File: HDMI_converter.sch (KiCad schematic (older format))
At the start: 106 parts, among them J2 46756-1001, Q1 BSS138APW, Q2 BSS138APW, Q3 BSS138APW, Q4 BSS138APW, U2 LT9611, U3 TXB0104RUT, U4 NTS0102GT, Y2 ABM8G-24.000MHZ-18-D2Y-T

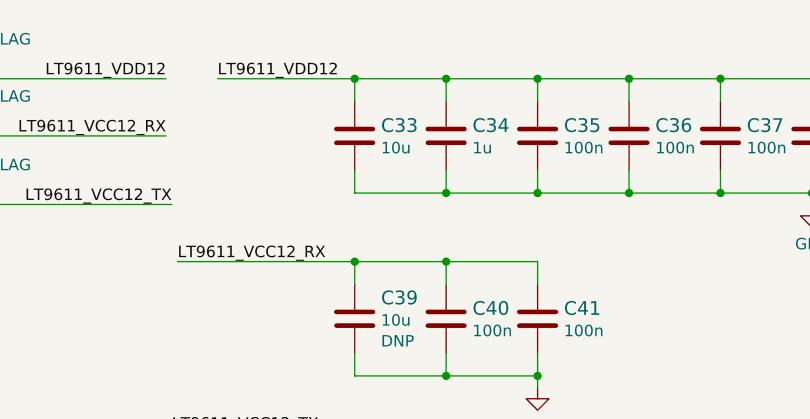
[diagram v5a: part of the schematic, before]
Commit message: Restore pcb with grouped parts. Change C33 to DNP
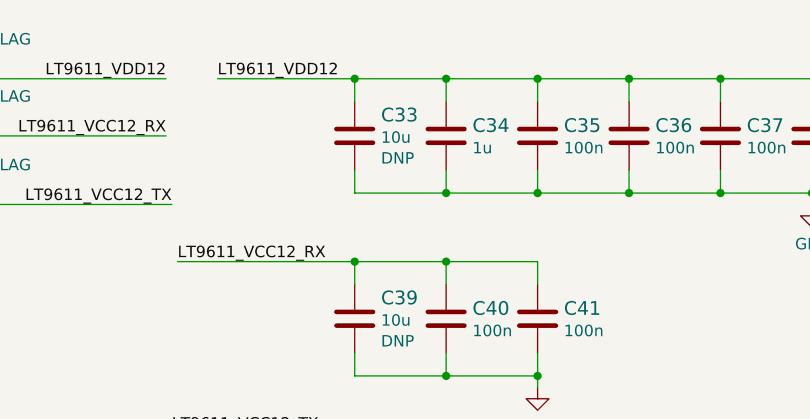
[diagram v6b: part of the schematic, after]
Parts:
- C33: DNP (none) -> DNP
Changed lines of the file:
@@
 U 1 1 627857E5
 P 8450 1150
-F 0 "C33" H 8565 1195 60  0000 L CNN
+F 0 "C33" H 8565 1241 60  0000 L CNN
 F 1 "C_10u_0402" H 8450 1000 60  0001 C CNN
 F 2 "sa800u-baseboard-hw-footprints:0402-cap" H 8650 1350 60  0001 L CNN
@@
 F 4 "MURATA" H 8650 1550 60  0001 L CNN "Manufacturer"
 F 5 "GRM155R60J106ME44D" H 8650 1450 60  0001 L CNN "MPN"
-F 6 "10u" H 8565 1097 50  0000 L CNN "Val"
+F 6 "10u" H 8565 1143 50  0000 L CNN "Val"
+F 7 "DNP" H 8565 1052 50  0000 L CNN "DNP"
 	1    8450 1150
 	1    0    0    -1

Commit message: Update 510R resistors
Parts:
- removed R134, R54, R56, R57, R58, R60, R61, R62: R_510R_0402, sa800u-baseboard-hw-footprints:0402-res, symbol sa800u-baseboard-hw:R_510R_0402
- added C151: C_100n_0402, sa800u-baseboard-hw-footprints:0402-cap, symbol sa800u-baseboard-hw:C_100n_0402
- added R134, R137, R57, R58, R60, R61, R62, R87: R_510R_0402, antmicro-footprints:0402-res, symbol antmicroResistors0402:R_510R_0402
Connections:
- wire segments 479 -> 483
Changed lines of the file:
@@
 Wire Wire Line
 	8850 1400 8450 1400
-Wire Wire Line
-	10450 1400 10450 1450
 $Comp
 L sa800u-baseboard-hw:GND #PWR019
 U 1 1 6271E8F1
-P 10450 1450
-F 0 "#PWR019" H 10450 1200 50  0001 C CNN
-F 1 "GND" H 10455 1277 50  0000 C CNN
-F 2 "" H 10450 1450 50  0001 C CNN
-F 3 "" H 10450 1450 50  0001 C CNN
-	1    10450 1450
+P 10850 1425
+F 0 "#PWR019" H 10850 1175 50  0001 C CNN
+F 1 "GND" H 10855 1252 50  0000 C CNN
+F 2 "" H 10850 1425 50  0001 C CNN
+F 3 "" H 10850 1425 50  0001 C CNN
+	1    10850 1425
 	1    0    0    -1
 $EndComp
@@
 	9325 6100 11600 6100
 Wire Wire Line
-	12475 6650 12475 6550
-Wire Wire Line
 	14575 6650 14575 6550
 Connection ~ 13525 6650
@@
 Wire Wire Line
 	3450 4125 3450 4025
-Connection ~ 10450 1400
 Connection ~ 8450 1700
 Connection ~ 8450 900
@@
 Wire Wire Line
 	2950 2475 3700 2475
-Text Label 2600 4025 0    50   ~ 0
+Text Label 2550 4425 0    50   ~ 0
 LT9611_VCC33_IO
-Text Label 2550 4425 0    50   ~ 0
+Text Label 2550 4025 0    50   ~ 0
 LT9611_VCC33_RX
 Text Label 2575 4725 0    50   ~ 0
@@
 	2550 4425 3450 4425
 Wire Wire Line
-	2600 4025 3450 4025
+	2550 4025 3450 4025
 Text Label 8600 4600 0    50   ~ 0
 LT9611_VCC33_TX
@@
 Wire Wire Line
 	4800 4925 5625 4925
-$Comp
-L sa800u-baseboard-hw:R_510R_0402 R54
-U 1 1 62E016CC
+Text GLabel 1375 6325 0    50   Input ~ 0
+DSI1_LN0_P
+$Comp
+L sa800u-baseboard-hw:C_100n_0402 C151
+U 1 1 620737ED
+P 10850 1150
+F 0 "C151" H 10965 1195 60  0000 L CNN
+F 1 "C_100n_0402" H 10850 1000 60  0001 C CNN
+F 2 "sa800u-baseboard-hw-footprints:0402-cap" H 11050 1350 60  0001 L CNN
+F 3 "" H 10850 1150 50  0001 C CNN
+F 4 "Walsin" H 11050 1550 60  0001 L CNN "Manufacturer"
+F 5 "0402X104K6R3CT" H 11050 1450 60  0001 L CNN "MPN"
+F 6 "100n" H 10965 1097 50  0000 L CNN "Val"
+	1    10850 1150
+	1    0    0    -1
+$EndComp
+Wire Wire Line
+	10850 900  10850 1000
+Wire Wire Line
+	10450 900  10850 900
+Wire Wire Line
+	10450 1400 10850 1400
+Connection ~ 10850 1400
+Wire Wire Line
+	10850 1400 10850 1425
+Wire Wire Line
+	10850 1300 10850 1400
+Connection ~ 10450 1400
+Connection ~ 10450 900
+$Comp
+L antmicroResistors0402:R_510R_0402 R57
+U 1 1 622FF01E
 P 12475 6400
-F 0 "R54" V 12430 6470 60  0000 L CNN
+F 0 "R57" V 12430 6470 60  0000 L CNN
 F 1 "R_510R_0402" H 12475 6250 60  0001 C CNN
-F 2 "sa800u-baseboard-hw-footprints:0402-res" H 12675 6600 60  0001 L CNN
+F 2 "antmicro-footprints:0402-res" H 12675 6600 60  0001 L CNN
 F 3 "" H 12475 6400 50  0001 C CNN
 F 4 "Yageo" H 12675 6800 60  0001 L CNN "Manufacturer"
@@
 	0    1    1    0
 $EndComp
-$Comp
-L sa800u-baseboard-hw:R_510R_0402 R56
-U 1 1 62E4D5ED
+Wire Wire Line
+	12475 6550 12475 6650
+$Comp
+L antmicroResistors0402:R_510R_0402 R58
+U 1 1 62395D6F
 P 12825 6400
-F 0 "R56" V 12780 6470 60  0000 L CNN
+F 0 "R58" V 12780 6470 60  0000 L CNN
 F 1 "R_510R_0402" H 12825 6250 60  0001 C CNN
-F 2 "sa800u-baseboard-hw-footprints:0402-res" H 13025 6600 60  0001 L CNN
+F 2 "antmicro-footprints:0402-res" H 13025 6600 60  0001 L CNN
 F 3 "" H 12825 6400 50  0001 C CNN
 F 4 "Yageo" H 13025 6800 60  0001 L CNN "Manufacturer"
@@
 $EndComp
 $Comp
-L sa800u-baseboard-hw:R_510R_0402 R57
-U 1 1 62E92C49
+L antmicroResistors0402:R_510R_0402 R60
+U 1 1 623DE328
 P 13175 6400
-F 0 "R57" V 13130 6470 60  0000 L CNN
+F 0 "R60" V 13130 6470 60  0000 L CNN
 F 1 "R_510R_0402" H 13175 6250 60  0001 C CNN
-F 2 "sa800u-baseboard-hw-footprints:0402-res" H 13375 6600 60  0001 L CNN
+F 2 "antmicro-footprints:0402-res" H 13375 6600 60  0001 L CNN
 F 3 "" H 13175 6400 50  0001 C CNN
 F 4 "Yageo" H 13375 6800 60  0001 L CNN "Manufacturer"
@@
 $EndComp
 $Comp
-L sa800u-baseboard-hw:R_510R_0402 R58
-U 1 1 62E92C52
+L antmicroResistors0402:R_510R_0402 R61
+U 1 1 623DE331
 P 13525 6400
-F 0 "R58" V 13480 6470 60  0000 L CNN
+F 0 "R61" V 13480 6470 60  0000 L CNN
 F 1 "R_510R_0402" H 13525 6250 60  0001 C CNN
-F 2 "sa800u-baseboard-hw-footprints:0402-res" H 13725 6600 60  0001 L CNN
+F 2 "antmicro-footprints:0402-res" H 13725 6600 60  0001 L CNN
 F 3 "" H 13525 6400 50  0001 C CNN
 F 4 "Yageo" H 13725 6800 60  0001 L CNN "Manufacturer"
@@
 $EndComp
 $Comp
-L sa800u-baseboard-hw:R_510R_0402 R60
-U 1 1 62ED7826
+L antmicroResistors0402:R_510R_0402 R62
+U 1 1 62423F3E
 P 13875 6400
-F 0 "R60" V 13830 6470 60  0000 L CNN
+F 0 "R62" V 13830 6470 60  0000 L CNN
 F 1 "R_510R_0402" H 13875 6250 60  0001 C CNN
-F 2 "sa800u-baseboard-hw-footprints:0402-res" H 14075 6600 60  0001 L CNN
+F 2 "antmicro-footprints:0402-res" H 14075 6600 60  0001 L CNN
 F 3 "" H 13875 6400 50  0001 C CNN
 F 4 "Yageo" H 14075 6800 60  0001 L CNN "Manufacturer"
@@
 $EndComp
 $Comp
-L sa800u-baseboard-hw:R_510R_0402 R61
-U 1 1 62ED782F
+L antmicroResistors0402:R_510R_0402 R87
+U 1 1 62423F47
 P 14225 6400
-F 0 "R61" V 14180 6470 60  0000 L CNN
+F 0 "R87" V 14180 6470 60  0000 L CNN
 F 1 "R_510R_0402" H 14225 6250 60  0001 C CNN
-F 2 "sa800u-baseboard-hw-footprints:0402-res" H 14425 6600 60  0001 L CNN
+F 2 "antmicro-footprints:0402-res" H 14425 6600 60  0001 L CNN
 F 3 "" H 14225 6400 50  0001 C CNN
 F 4 "Yageo" H 14425 6800 60  0001 L CNN "Manufacturer"
@@
 $EndComp
 $Comp
-L sa800u-baseboard-hw:R_510R_0402 R62
-U 1 1 62F1C359
+L antmicroResistors0402:R_510R_0402 R134
+U 1 1 624698FA
 P 14575 6400
-F 0 "R62" V 14530 6470 60  0000 L CNN
+F 0 "R134" V 14530 6470 60  0000 L CNN
 F 1 "R_510R_0402" H 14575 6250 60  0001 C CNN
-F 2 "sa800u-baseboard-hw-footprints:0402-res" H 14775 6600 60  0001 L CNN
+F 2 "antmicro-footprints:0402-res" H 14775 6600 60  0001 L CNN
 F 3 "" H 14575 6400 50  0001 C CNN
 F 4 "Yageo" H 14775 6800 60  0001 L CNN "Manufacturer"
@@
 $EndComp
 $Comp
-L sa800u-baseboard-hw:R_510R_0402 R134
-U 1 1 62F1C362
+L antmicroResistors0402:R_510R_0402 R137
+U 1 1 62469903
 P 14925 6400
-F 0 "R134" V 14880 6470 60  0000 L CNN
+F 0 "R137" V 14880 6470 60  0000 L CNN
 F 1 "R_510R_0402" H 14925 6250 60  0001 C CNN
-F 2 "sa800u-baseboard-hw-footprints:0402-res" H 15125 6600 60  0001 L CNN
+F 2 "antmicro-footprints:0402-res" H 15125 6600 60  0001 L CNN
 F 3 "" H 14925 6400 50  0001 C CNN
 F 4 "Yageo" H 15125 6800 60  0001 L CNN "Manufacturer"
@@
 	0    1    1    0
 $EndComp
-Text GLabel 1375 6325 0    50   Input ~ 0
-DSI1_LN0_P
 $EndSCHEMATC

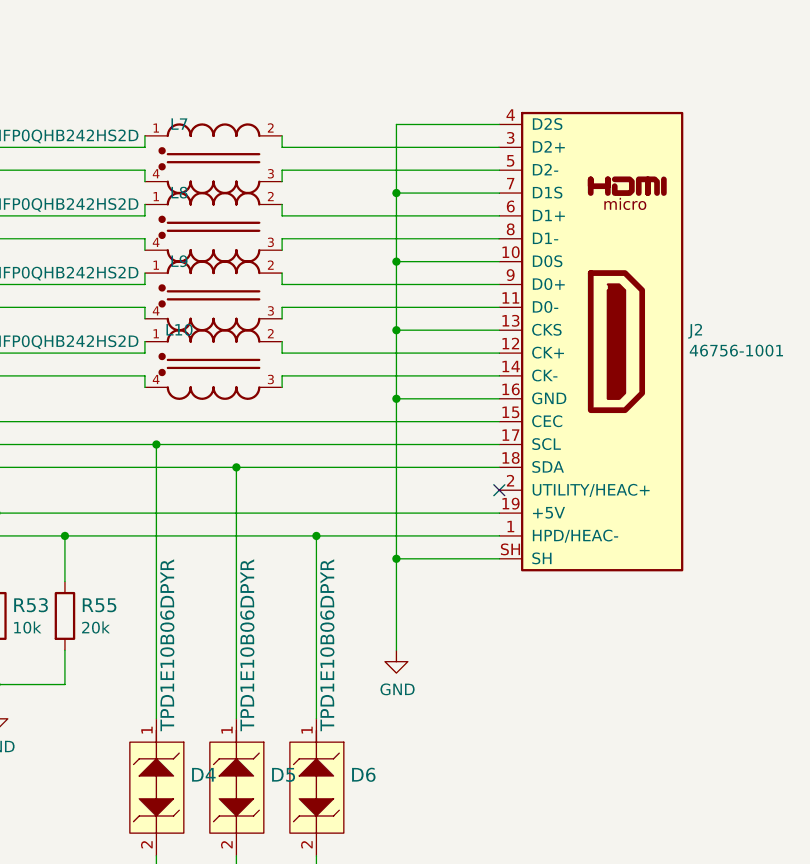
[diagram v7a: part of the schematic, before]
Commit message: Add names to nets connected to HDMI connector
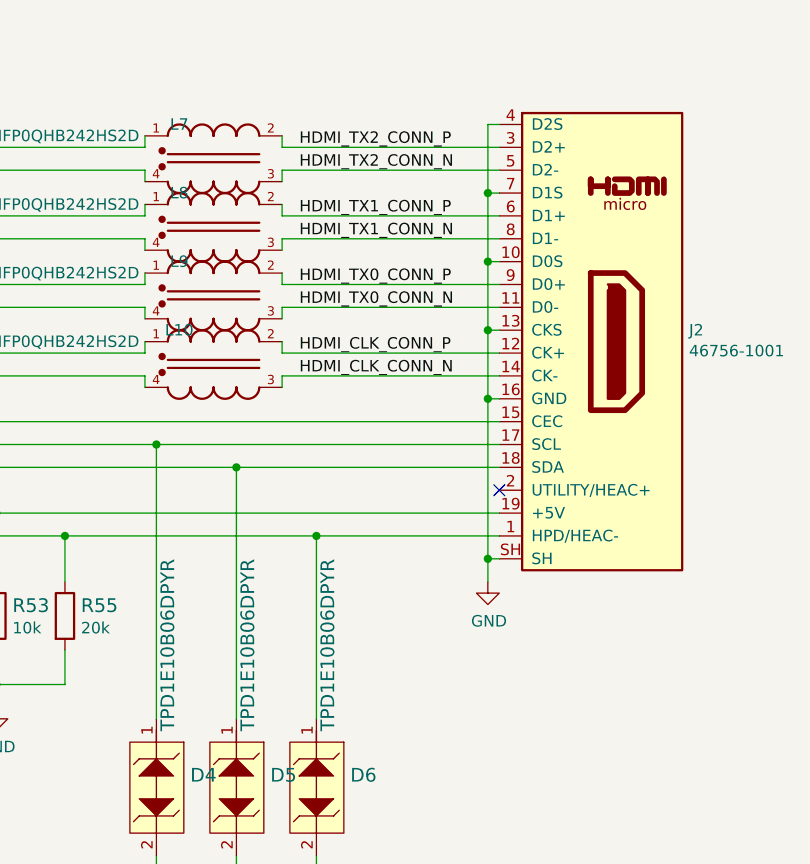
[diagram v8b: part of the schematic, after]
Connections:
- net HDMI_TX0_CONN_N: now reaches J2.11 (D0-), L9.3
- net HDMI_CLK_CONN_P: now reaches J2.12 (CK+), L10.2
- net HDMI_CLK_CONN_N: now reaches J2.14 (CK-), L10.3
- net HDMI_TX2_CONN_P: now reaches J2.3 (D2+), L7.2
- net HDMI_TX2_CONN_N: now reaches J2.5 (D2-), L7.3
- net HDMI_TX1_CONN_P: now reaches J2.6 (D1+), L8.2
- net HDMI_TX1_CONN_N: now reaches J2.8 (D1-), L8.3
- net HDMI_TX0_CONN_P: now reaches J2.9 (D0+), L9.2
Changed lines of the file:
@@
 HDMI_CLK_N
 Wire Wire Line
-	14750 1100 14300 1100
-Wire Wire Line
-	14300 1100 14300 1400
-Wire Wire Line
-	14750 3000 14300 3000
+	14750 3000 14700 3000
 Wire Wire Line
 	14750 1200 13800 1200
@@
 $EndComp
 Wire Wire Line
-	14750 1400 14300 1400
-Connection ~ 14300 1400
-Wire Wire Line
-	14300 1400 14300 1700
+	14750 1400 14700 1400
 Wire Wire Line
 	14750 1500 13800 1500
@@
 $EndComp
 Wire Wire Line
-	14750 1700 14300 1700
-Connection ~ 14300 1700
-Wire Wire Line
-	14300 1700 14300 2000
-Wire Wire Line
 	14750 1800 13800 1800
 Wire Wire Line
@@
 	1    0    0    -1
 $EndComp
-Wire Wire Line
-	14750 2000 14300 2000
 Wire Wire Line
 	14750 2100 13800 2100
@@
 	1    0    0    -1
 $EndComp
-Wire Wire Line
-	14300 2000 14300 2300
-Connection ~ 14300 2000
-Connection ~ 14300 3000
 Text Label 11850 2800 0    50   ~ 0
 5V_HDMI
@@
 Wire Wire Line
 	11850 2800 12550 2800
-Wire Wire Line
-	14300 3000 14300 3400
 $Comp
 L sa800u-baseboard-hw:GND #PWR035
 U 1 1 62C195C0
-P 14300 3400
-F 0 "#PWR035" H 14300 3150 50  0001 C CNN
-F 1 "GND" H 14305 3227 50  0000 C CNN
-F 2 "" H 14300 3400 50  0001 C CNN
-F 3 "" H 14300 3400 50  0001 C CNN
-	1    14300 3400
-	1    0    0    -1
-$EndComp
-Wire Wire Line
-	14750 2300 14300 2300
-Connection ~ 14300 2300
-Wire Wire Line
-	14300 2300 14300 3000
+P 14700 3100
+F 0 "#PWR035" H 14700 2850 50  0001 C CNN
+F 1 "GND" H 14705 2927 50  0000 C CNN
+F 2 "" H 14700 3100 50  0001 C CNN
+F 3 "" H 14700 3100 50  0001 C CNN
+	1    14700 3100
+	1    0    0    -1
+$EndComp
 $Comp
 L sa800u-baseboard-hw:BSS138APW Q4
@@
 	0    1    1    0
 $EndComp
+Text Label 13875 1200 0    50   ~ 0
+HDMI_TX2_CONN_P
+Text Label 13875 1300 0    50   ~ 0
+HDMI_TX2_CONN_N
+Text Label 13875 1500 0    50   ~ 0
+HDMI_TX1_CONN_P
+Text Label 13875 1600 0    50   ~ 0
+HDMI_TX1_CONN_N
+Text Label 13875 1800 0    50   ~ 0
+HDMI_TX0_CONN_P
+Text Label 13875 1900 0    50   ~ 0
+HDMI_TX0_CONN_N
+Text Label 13875 2100 0    50   ~ 0
+HDMI_CLK_CONN_P
+Text Label 13875 2200 0    50   ~ 0
+HDMI_CLK_CONN_N
+Wire Wire Line
+	14700 1100 14700 1400
+Wire Wire Line
+	14700 1100 14750 1100
+Connection ~ 14700 1400
+Wire Wire Line
+	14700 1400 14700 1700
+Connection ~ 14700 3000
+Connection ~ 14700 2300
+Wire Wire Line
+	14700 2300 14700 3000
+Wire Wire Line
+	14700 2300 14750 2300
+Connection ~ 14700 2000
+Wire Wire Line
+	14700 2000 14700 2300
+Wire Wire Line
+	14700 2000 14750 2000
+Connection ~ 14700 1700
+Wire Wire Line
+	14700 1700 14700 2000
+Wire Wire Line
+	14700 1700 14750 1700
+Wire Wire Line
+	14700 3000 14700 3100
 $EndSCHEMATC
